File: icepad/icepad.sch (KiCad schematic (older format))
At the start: 56 parts, among them J1 Conn_01x04, J2 USB_B_Mini, U1 STM32F042K6Tx, U2 USBLC6-2SC6, U3 TLV62568DRL

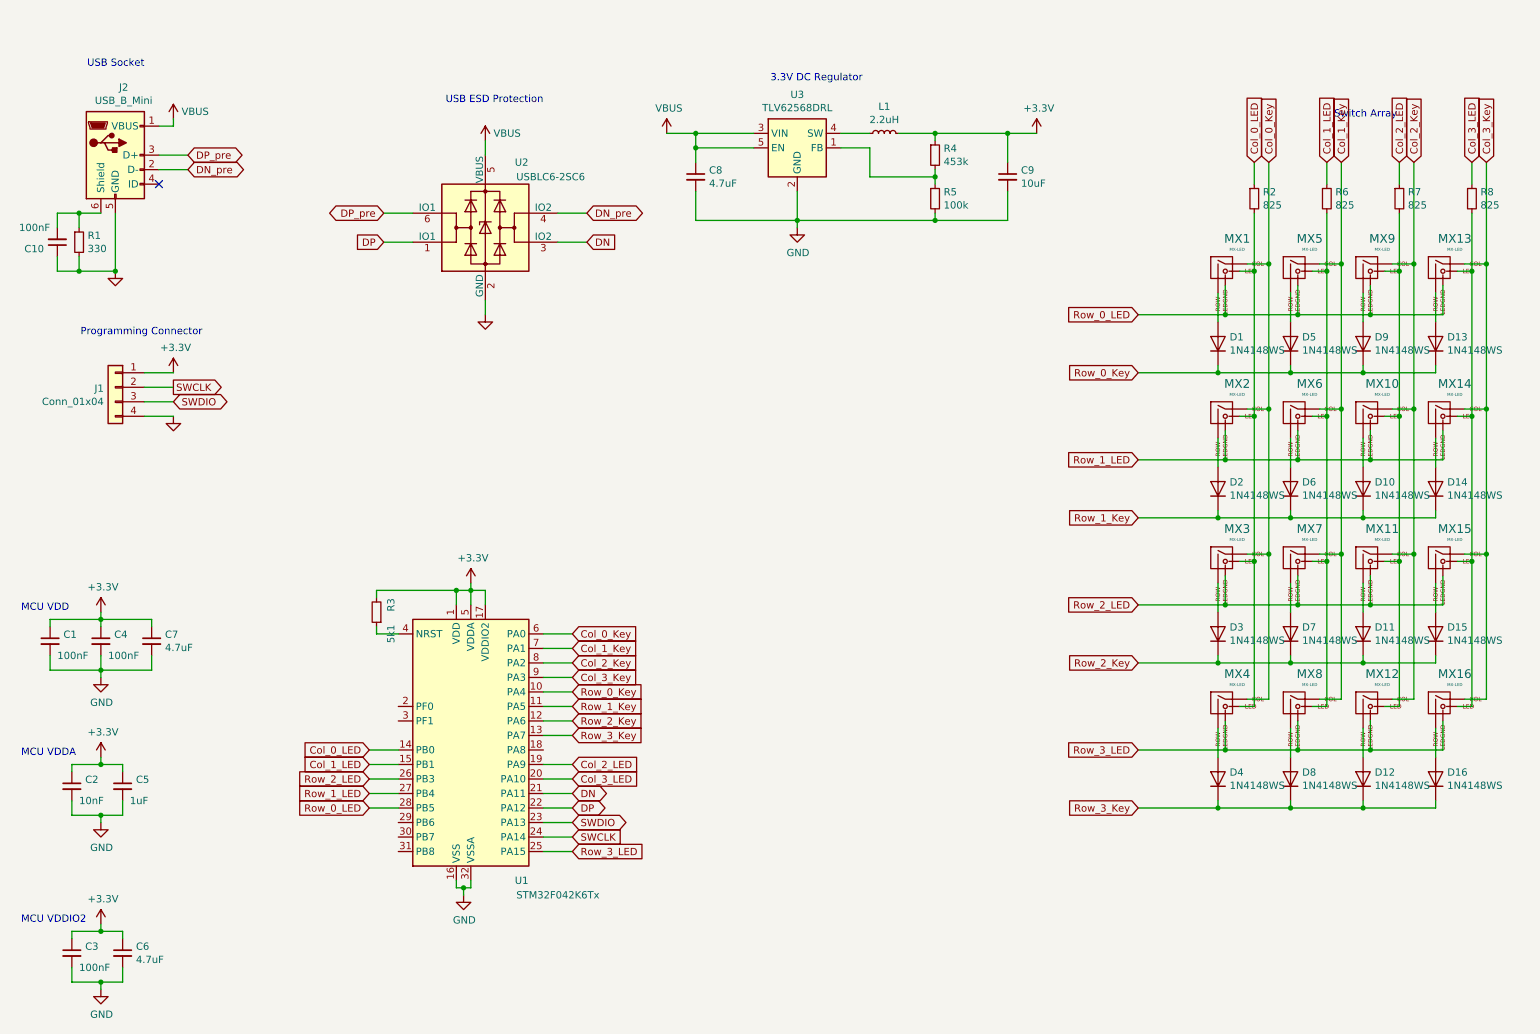
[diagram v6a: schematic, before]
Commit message: added potentiometers and 3d models
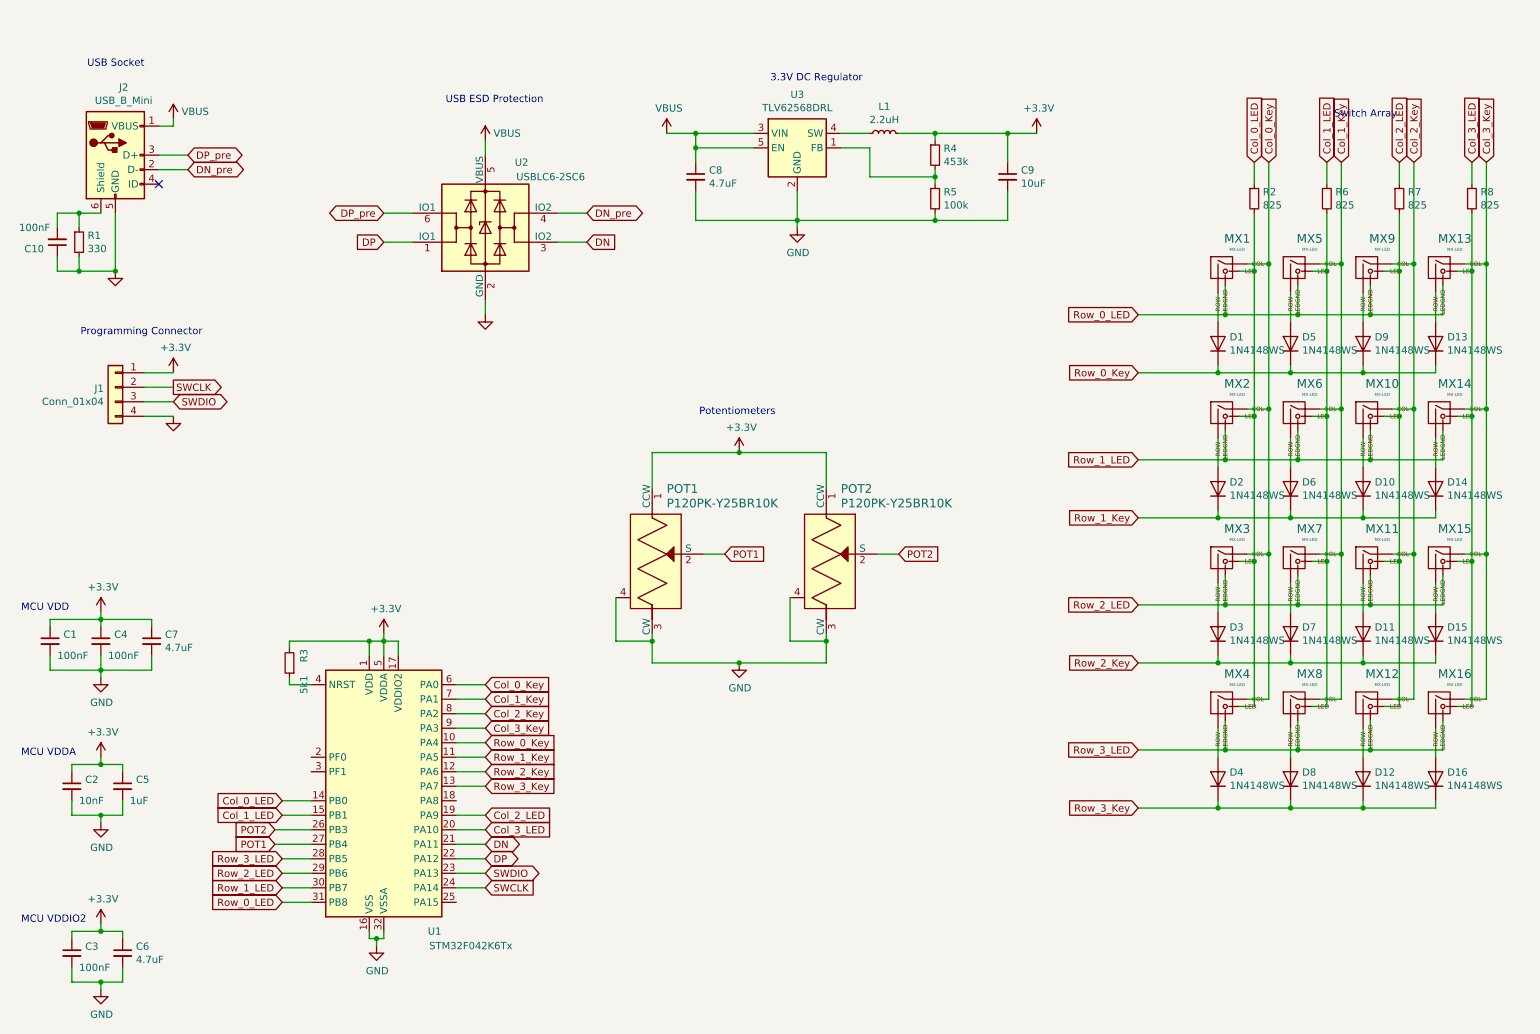
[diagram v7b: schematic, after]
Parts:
- added POT1, POT2: P120PK-Y25BR10K, pot:Potentiometer_P120PK-Y25BR10K, symbol dk_Rotary-Potentiometers-Rheostats:P120PK-Y25BR10K
- J2: footprint digikey-footprints:USB_Mini_B_Female_548190519 -> usb:USB_Mini_B_Female_548190519
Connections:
- net +3V3: now also POT1.1 (CCW), POT2.1 (CCW)
- net GND: now also POT1.3 (CW), POT1.4, POT2.3 (CW), POT2.4
- net Row_0_LED: now also U1.31 (PB8); no longer U1.28 (PB5)
- net Row_1_LED: now also U1.30 (PB7); no longer U1.27 (PB4)
- net Row_2_LED: now also U1.29 (PB6); no longer U1.26 (PB3)
- net Row_3_LED: now also U1.28 (PB5); no longer U1.25 (PA15)
- new net POT1: POT1.2 (S), U1.27 (PB4)
- new net POT2: POT2.2 (S), U1.26 (PB3)
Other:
- note added: "Potentiometers"
- moved on the sheet: R3, U1

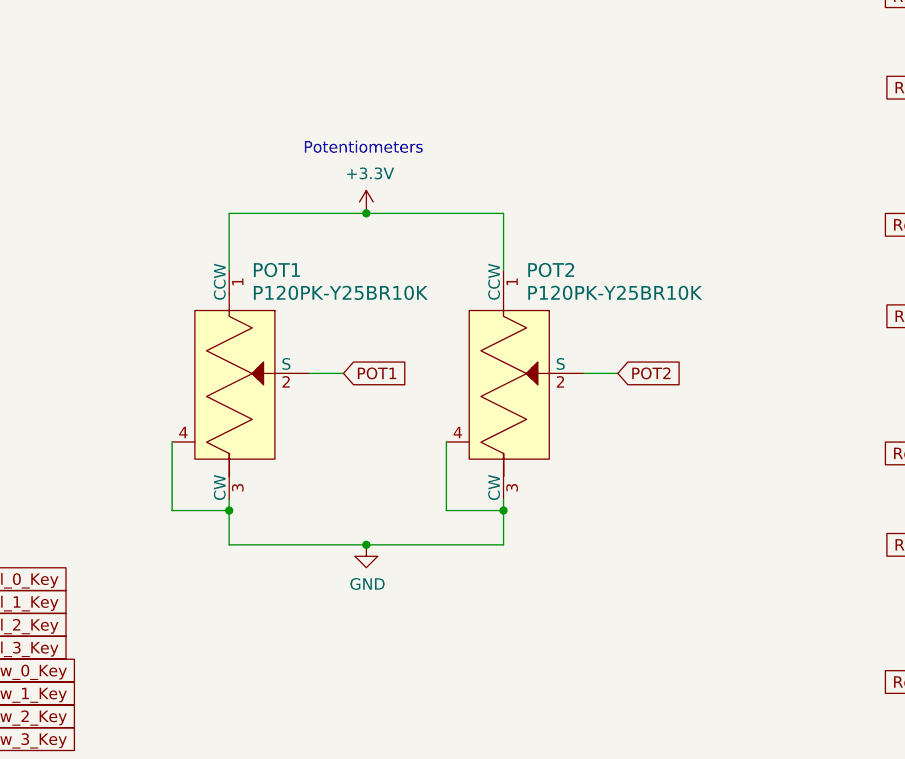
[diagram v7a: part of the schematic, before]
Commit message: changed potentiometer
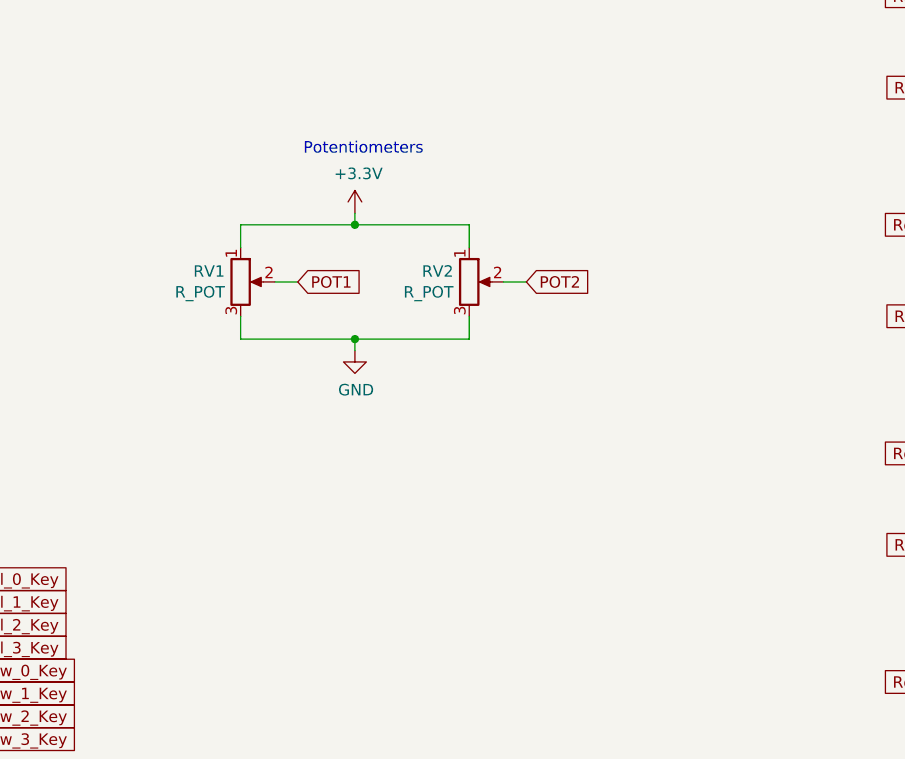
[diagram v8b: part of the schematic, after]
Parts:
- removed POT1, POT2: P120PK-Y25BR10K, pot:Potentiometer_P120PK-Y25BR10K, symbol dk_Rotary-Potentiometers-Rheostats:P120PK-Y25BR10K
- added RV1, RV2: R_POT, pot:RK09K1130A5R, symbol Device:R_POT
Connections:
- net +3V3: now also RV1.1, RV2.1
- net GND: now also RV1.3, RV2.3
- net POT1: now also RV1.2
- net POT2: now also RV2.2
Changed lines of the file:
@@
 Wire Wire Line
 	10800 2100 10800 3100
-$Comp
-L dk_Rotary-Potentiometers-Rheostats:P120PK-Y25BR10K POT1
-U 1 1 5EA30879
-P 5150 4050
-F 0 "POT1" V 4700 4150 60  0000 L CNN
-F 1 "P120PK-Y25BR10K" V 4800 4150 60  0000 L CNN
-F 2 "pot:Potentiometer_P120PK-Y25BR10K" H 5350 4250 60  0001 L CNN
-F 3 "https://www.ttelectronics.com/TTElectronics/media/ProductFiles/Potentiometers/Datasheets/P120.pdf" H 5350 4350 60  0001 L CNN
-F 4 "987-1710-ND" H 5350 4450 60  0001 L CNN "Digi-Key_PN"
-F 5 "P120PK-Y25BR10K" H 5350 4550 60  0001 L CNN "MPN"
-F 6 "Potentiometers, Variable Resistors" H 5350 4650 60  0001 L CNN "Category"
-F 7 "Rotary Potentiometers, Rheostats" H 5350 4750 60  0001 L CNN "Family"
-F 8 "https://www.ttelectronics.com/TTElectronics/media/ProductFiles/Potentiometers/Datasheets/P120.pdf" H 5350 4850 60  0001 L CNN "DK_Datasheet_Link"
-F 9 "/product-detail/en/tt-electronics-bi/P120PK-Y25BR10K/987-1710-ND/5957454" H 5350 4950 60  0001 L CNN "DK_Detail_Page"
-F 10 "POT 10K OHM 1/20W PLASTIC LINEAR" H 5350 5050 60  0001 L CNN "Description"
-F 11 "TT Electronics/BI" H 5350 5150 60  0001 L CNN "Manufacturer"
-F 12 "Active" H 5350 5250 60  0001 L CNN "Status"
-	1    5150 4050
-	0    1    1    0
-$EndComp
 Wire Wire Line
 	2800 5850 2600 5850
@@
 Wire Wire Line
 	2550 6050 2800 6050
-$Comp
-L dk_Rotary-Potentiometers-Rheostats:P120PK-Y25BR10K POT2
-U 1 1 5EB05CCF
-P 6350 4050
-F 0 "POT2" V 5900 4150 60  0000 L CNN
-F 1 "P120PK-Y25BR10K" V 6000 4150 60  0000 L CNN
-F 2 "pot:Potentiometer_P120PK-Y25BR10K" H 6550 4250 60  0001 L CNN
-F 3 "https://www.ttelectronics.com/TTElectronics/media/ProductFiles/Potentiometers/Datasheets/P120.pdf" H 6550 4350 60  0001 L CNN
-F 4 "987-1710-ND" H 6550 4450 60  0001 L CNN "Digi-Key_PN"
-F 5 "P120PK-Y25BR10K" H 6550 4550 60  0001 L CNN "MPN"
-F 6 "Potentiometers, Variable Resistors" H 6550 4650 60  0001 L CNN "Category"
-F 7 "Rotary Potentiometers, Rheostats" H 6550 4750 60  0001 L CNN "Family"
-F 8 "https://www.ttelectronics.com/TTElectronics/media/ProductFiles/Potentiometers/Datasheets/P120.pdf" H 6550 4850 60  0001 L CNN "DK_Datasheet_Link"
-F 9 "/product-detail/en/tt-electronics-bi/P120PK-Y25BR10K/987-1710-ND/5957454" H 6550 4950 60  0001 L CNN "DK_Detail_Page"
-F 10 "POT 10K OHM 1/20W PLASTIC LINEAR" H 6550 5050 60  0001 L CNN "Description"
-F 11 "TT Electronics/BI" H 6550 5150 60  0001 L CNN "Manufacturer"
-F 12 "Active" H 6550 5250 60  0001 L CNN "Status"
-	1    6350 4050
-	0    1    1    0
-$EndComp
 Text GLabel 2550 5950 0    50   Input ~ 0
 POT2
 Wire Wire Line
 	2550 5950 2800 5950
-Text GLabel 6850 4050 2    50   Input ~ 0
+Text GLabel 6450 3650 2    50   Input ~ 0
 POT2
-Text GLabel 5650 4050 2    50   Input ~ 0
+Text GLabel 5450 3650 2    50   Input ~ 0
 POT1
-Wire Wire Line
-	5650 4050 5500 4050
-Wire Wire Line
-	6850 4050 6700 4050
+Text Notes 6000 3100 2    50   ~ 0
+Potentiometers
+$Comp
+L Device:R_POT RV1
+U 1 1 5EC75694
+P 5200 3650
+F 0 "RV1" H 5131 3696 50  0000 R CNN
+F 1 "R_POT" H 5131 3605 50  0000 R CNN
+F 2 "pot:RK09K1130A5R" H 5200 3650 50  0001 C CNN
+F 3 "~" H 5200 3650 50  0001 C CNN
+	1    5200 3650
+	1    0    0    -1
+$EndComp
+$Comp
+L Device:R_POT RV2
+U 1 1 5EC75DC8
+P 6200 3650
+F 0 "RV2" H 6131 3696 50  0000 R CNN
+F 1 "R_POT" H 6131 3605 50  0000 R CNN
+F 2 "pot:RK09K1130A5R" H 6200 3650 50  0001 C CNN
+F 3 "~" H 6200 3650 50  0001 C CNN
+	1    6200 3650
+	1    0    0    -1
+$EndComp
 $Comp
 L power:+3.3V #PWR0103
-U 1 1 5EB9A590
-P 5750 3350
-F 0 "#PWR0103" H 5750 3200 50  0001 C CNN
-F 1 "+3.3V" H 5765 3523 50  0000 C CNN
-F 2 "" H 5750 3350 50  0001 C CNN
-F 3 "" H 5750 3350 50  0001 C CNN
-	1    5750 3350
+U 1 1 5EC761F1
+P 5700 3350
+F 0 "#PWR0103" H 5700 3200 50  0001 C CNN
+F 1 "+3.3V" H 5715 3523 50  0000 C CNN
+F 2 "" H 5700 3350 50  0001 C CNN
+F 3 "" H 5700 3350 50  0001 C CNN
+	1    5700 3350
 	1    0    0    -1
 $EndComp
 $Comp
 L power:GND #PWR0104
-U 1 1 5EB9AB2B
-P 5750 4800
-F 0 "#PWR0104" H 5750 4550 50  0001 C CNN
-F 1 "GND" H 5755 4627 50  0000 C CNN
-F 2 "" H 5750 4800 50  0001 C CNN
-F 3 "" H 5750 4800 50  0001 C CNN
-	1    5750 4800
+U 1 1 5EC7665F
+P 5700 3950
+F 0 "#PWR0104" H 5700 3700 50  0001 C CNN
+F 1 "GND" H 5705 3777 50  0000 C CNN
+F 2 "" H 5700 3950 50  0001 C CNN
+F 3 "" H 5700 3950 50  0001 C CNN
+	1    5700 3950
 	1    0    0    -1
 $EndComp
 Wire Wire Line
-	5750 4800 6350 4800
+	5200 3800 5200 3900
 Wire Wire Line
-	6350 4800 6350 4650
+	5700 3950 5700 3900
 Wire Wire Line
-	5750 4800 5150 4800
+	5700 3900 5200 3900
 Wire Wire Line
-	5150 4800 5150 4650
-Connection ~ 5750 4800
+	5700 3900 6200 3900
 Wire Wire Line
-	5150 3600 5150 3350
+	6200 3900 6200 3800
+Connection ~ 5700 3900
 Wire Wire Line
-	5150 3350 5750 3350
+	6200 3500 6200 3400
 Wire Wire Line
-	5750 3350 6350 3350
+	6200 3400 5700 3400
 Wire Wire Line
-	6350 3350 6350 3600
-Connection ~ 5750 3350
-Text Notes 6000 3100 2    50   ~ 0
-Potentiometers
+	5700 3400 5700 3350
 Wire Wire Line
-	4900 4350 4900 4650
+	5200 3500 5200 3400
 Wire Wire Line
-	4900 4650 5150 4650
-Connection ~ 5150 4650
+	5200 3400 5700 3400
+Connection ~ 5700 3400
 Wire Wire Line
-	5150 4650 5150 4600
+	5450 3650 5350 3650
 Wire Wire Line
-	6100 4350 6100 4650
-Wire Wire Line
-	6100 4650 6350 4650
-Connection ~ 6350 4650
-Wire Wire Line
-	6350 4650 6350 4600
+	6350 3650 6450 3650
 $EndSCHEMATC
